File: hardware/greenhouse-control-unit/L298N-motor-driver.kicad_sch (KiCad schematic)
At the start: 16 parts, among them Q12 D44H8, U3 L7810, U4 L298HN

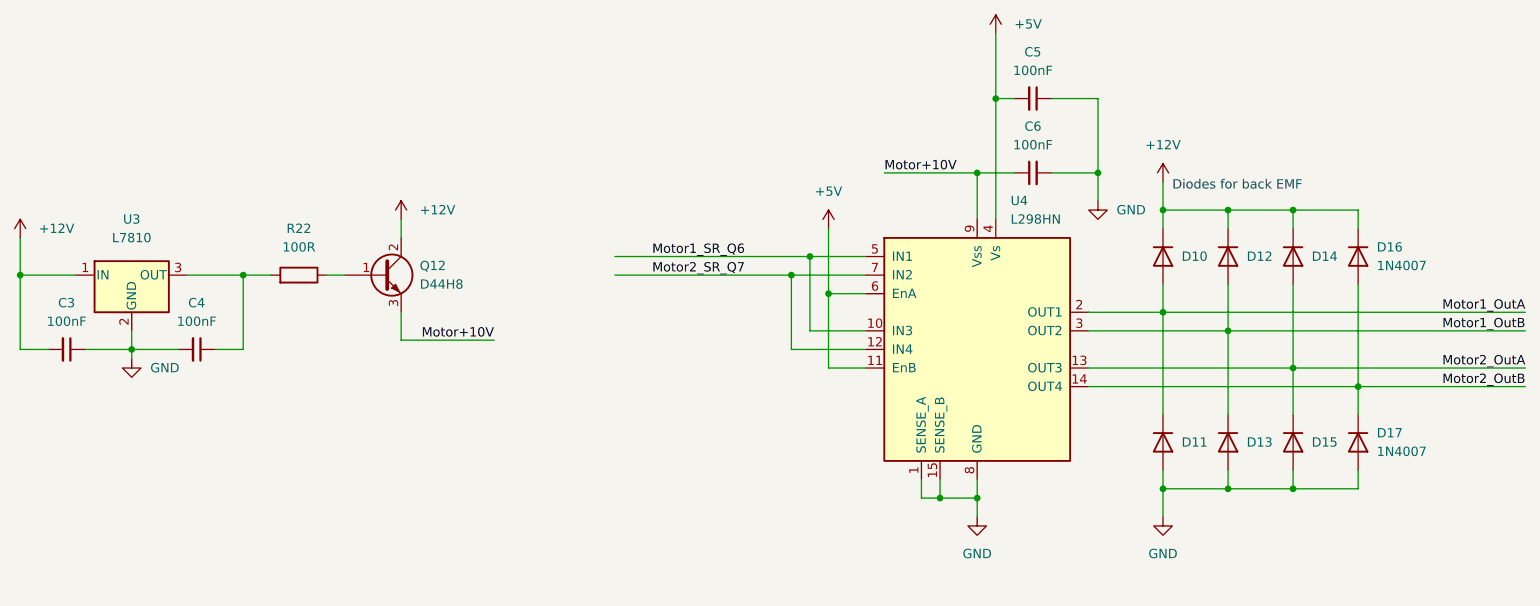
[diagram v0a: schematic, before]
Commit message: Remove small buck
Also:
- Change source to 10V
- Use 5V for radios
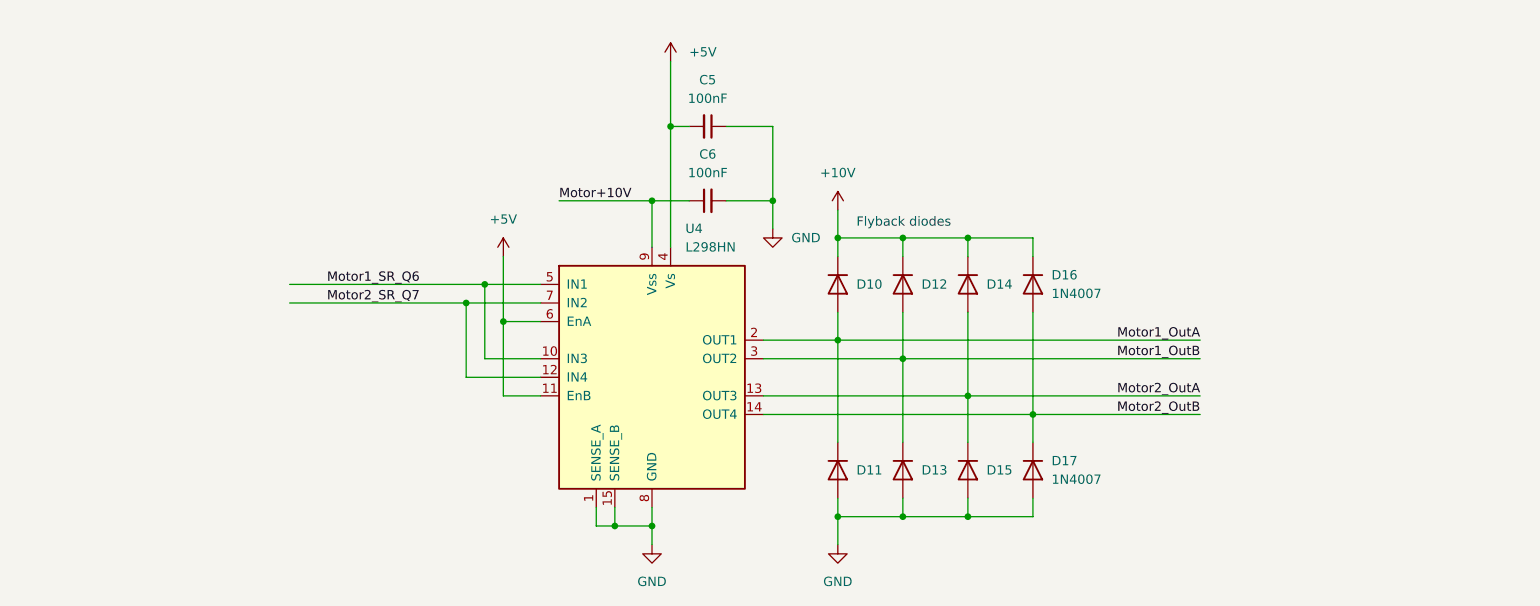
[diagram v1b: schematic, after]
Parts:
- removed C3, C4: 100nF, Capacitor_THT:C_Disc_D4.7mm_W2.5mm_P5.00mm, symbol Device:C_Small
- removed Q12: D44H8, Package_TO_SOT_THT:TO-220-3_Vertical, symbol Transistor_BJT:BD911
- removed R22: 100R, Resistor_THT:R_Axial_DIN0204_L3.6mm_D1.6mm_P5.08mm_Horizontal, symbol Device:R
- removed U3: L7810, Nick:TO-92L_Inline_Regulator, symbol Regulator_Linear:L7809
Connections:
- net +12V renamed +10V
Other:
- note added: "Flyback diodes"
- note removed: "Diodes for back EMF"
- moved on the sheet: C5, C6, D10, D11, D12, D13, D14, D15, D16, D17, U4
